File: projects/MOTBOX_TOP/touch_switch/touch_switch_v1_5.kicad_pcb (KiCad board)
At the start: 2 copper layers, 19 x 41.8 mm, 14 parts, among them J1 Conn_01x04, U1 TTP223

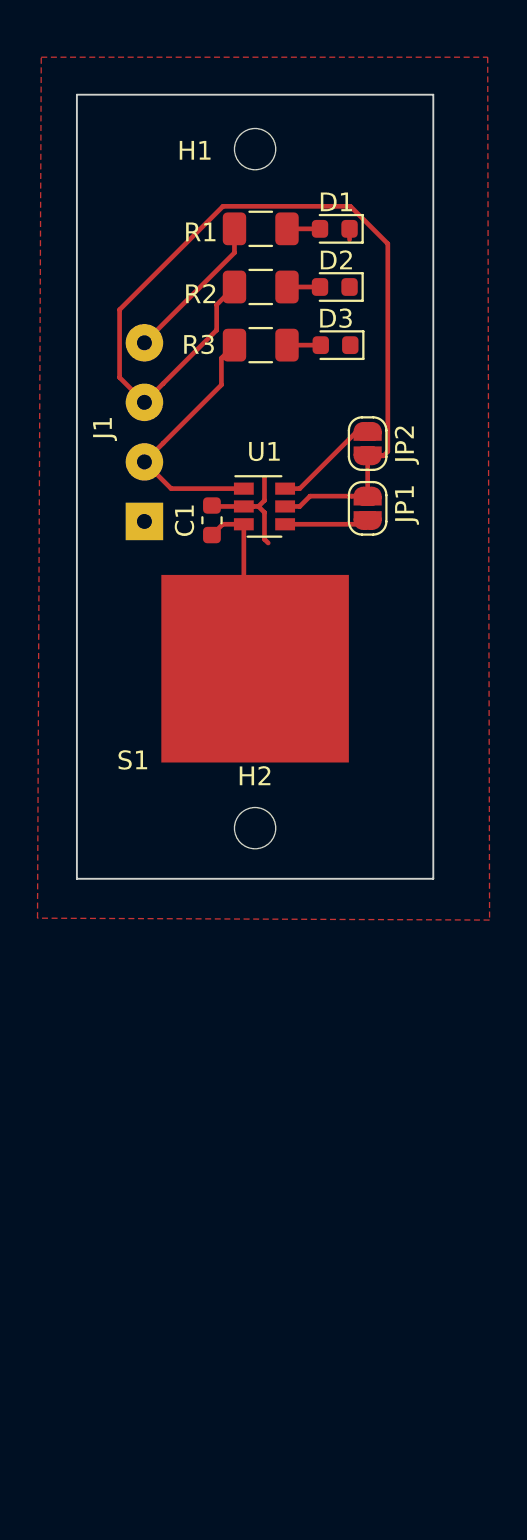
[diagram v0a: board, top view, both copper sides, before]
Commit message: Switch PCB is now of 80mm
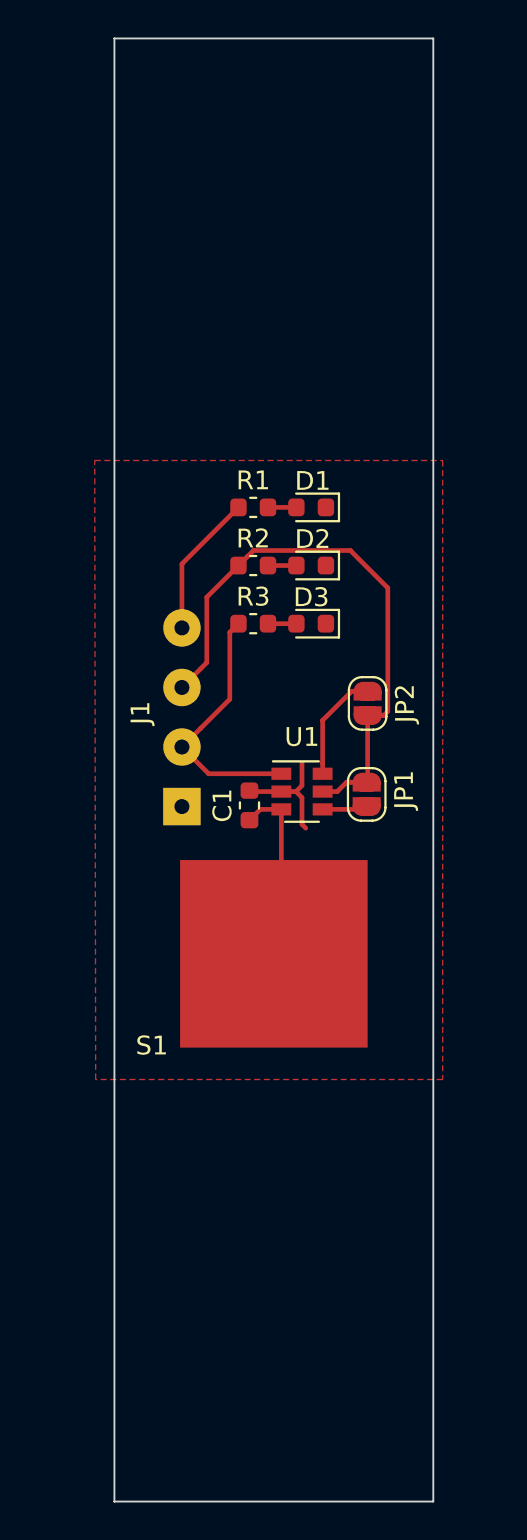
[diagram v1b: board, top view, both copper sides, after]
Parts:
- removed H1, H2: MountingHole, MountingHole:MountingHole_2.2mm_M2_ISO7380
- D1: value LED_Small -> LED_RED
- D2: value LED_Small -> LED_GREEN
- D3: value LED_Small -> LED_BLUE
- R1, R2, R3: value 150R -> 150E; footprint Resistor_SMD:R_1206_3216Metric -> Resistor_SMD:R_0603_1608Metric
- moved C1 15.3 mm to (113.2, 110.9)
- moved J1 15.3 mm to (109.6, 111.0)
- moved U1 15.3 mm to (116.0, 110.2)
- moved JP1 15.3 mm to (119.5, 110.3)
- moved S1 15.2 mm to (114.5, 118.8)
- moved D3 14.9 mm to (116.5, 101.2)
- moved D1 14.9 mm to (116.5, 95.0)
- moved D2 14.9 mm to (116.5, 98.1)
- moved R3 14.9 mm to (113.4, 101.2)
- moved R1 14.9 mm to (113.4, 95.0)
- moved R2 14.9 mm to (113.4, 98.1)
- moved JP2 13.9 mm to (119.5, 105.5)
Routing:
- net Net-(J1-Pad3): track 50.1 -> 30.7 mm
- net Net-(JP1-Pad1): track 4.48 -> 2.41 mm
- net Net-(C1-Pad1): track 11.4 -> 13.1 mm
- net Net-(C1-Pad2): track 7.47 -> 6.84 mm
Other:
- board size 19 x 41.8 mm -> 17 x 78 mm
- board text added: "LED Display area"
- board text added: "Touch Panel"

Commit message: Changes misc
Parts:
- D2: value LED_GREEN -> LED_BLUE
- D3: value LED_BLUE -> LED_GREEN
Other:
- board text added: "GND"
- board text added: "Touch Switch NU V1.5"
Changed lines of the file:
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@@
   (general
     (thickness 1.6)
-    (drawings 27)
+    (drawings 29)
     (tracks 48)
     (zones 0)
@@
     (46 B.CrtYd user)
     (47 F.CrtYd user)
-    (48 B.Fab user hide)
+    (48 B.Fab user)
     (49 F.Fab user hide)
   )
@@
       (effects (font (size 1 1) (thickness 0.15)))
     )
-    (fp_text value LED_RED (at 0 1.43 180) (layer F.Fab)
+    (fp_text value LED_RED (at -4.8125 -0.1 180) (layer F.Fab)
       (effects (font (size 1 1) (thickness 0.15)))
     )
@@
       (effects (font (size 1 1) (thickness 0.15)))
     )
-    (fp_text value LED_GREEN (at 0 1.43 180) (layer F.Fab)
+    (fp_text value LED_BLUE (at -5.2125 -0.1 180) (layer F.Fab)
       (effects (font (size 1 1) (thickness 0.15)))
     )
@@
       (effects (font (size 1 1) (thickness 0.15)))
     )
-    (fp_text value LED_BLUE (at 0 1.43 180) (layer F.Fab)
+    (fp_text value LED_GREEN (at -5.8625 0 180) (layer F.Fab)
       (effects (font (size 1 1) (thickness 0.15)))
     )
@@
     )
   )
+  (gr_text GND (at 107.5 111.175 90) (layer F.SilkS)
+    (effects (font (size 1 1) (thickness 0.25)))
+  )
+  (gr_text "Touch Switch\nNU V1.5" (at 113.975 144.3) (layer F.SilkS)
+    (effects (font (size 1 1) (thickness 0.25)))
+  )
   (gr_text "LED Display \narea" (at 138.8 98.3) (layer Cmts.User)
